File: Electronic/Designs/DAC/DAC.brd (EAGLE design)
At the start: 50 x 50 mm, 37 parts

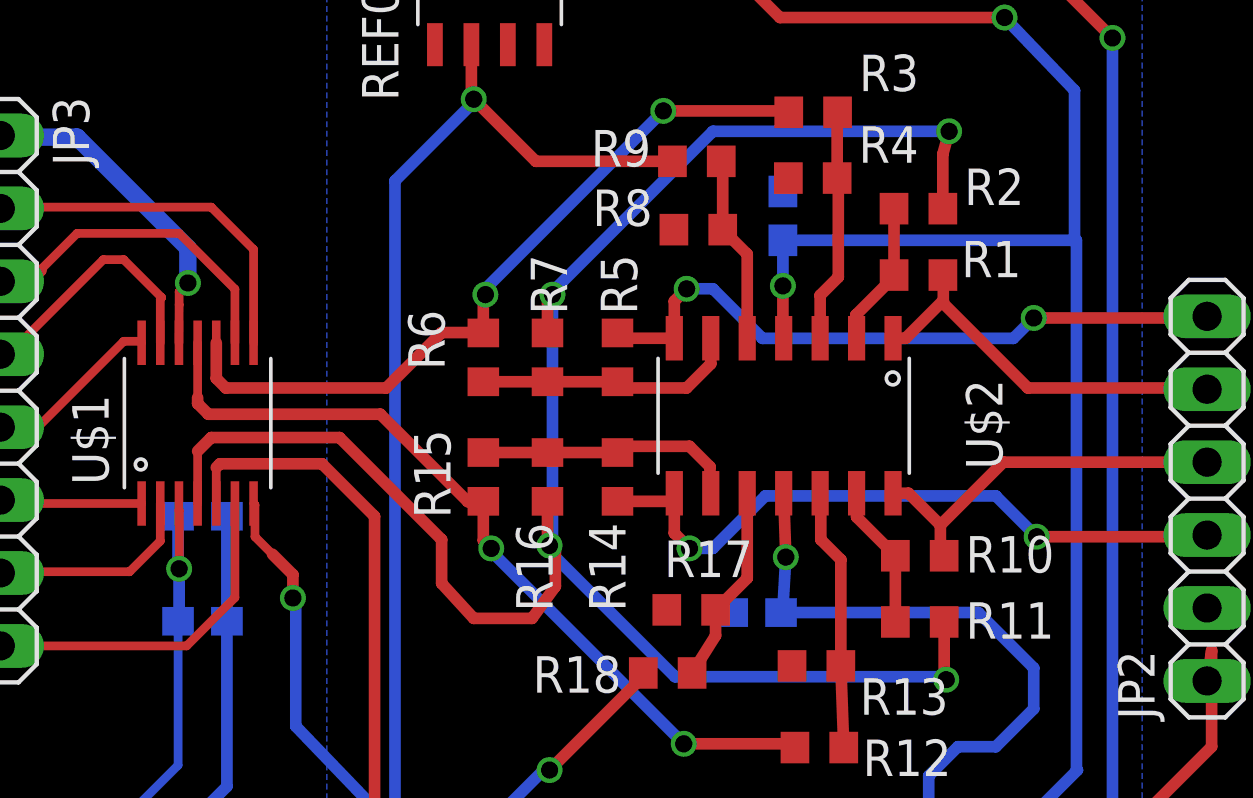
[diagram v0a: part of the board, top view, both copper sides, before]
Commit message: added dirt cheap drc / cam files , minor fix to board dac
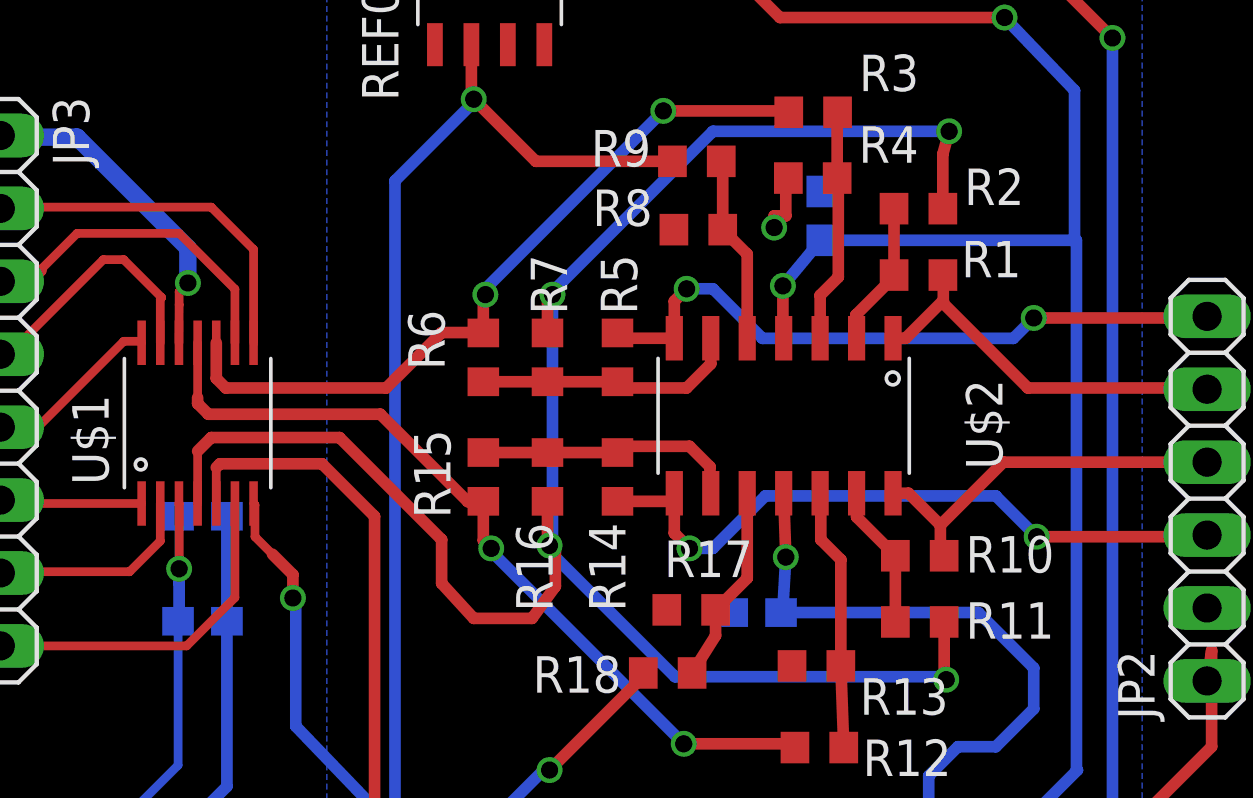
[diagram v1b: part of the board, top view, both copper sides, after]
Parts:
- moved C4 1.32 mm to (32.2, 33.3)
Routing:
- net GND: track 33.6 -> 36.3 mm, vias 1 -> 2
- net +15V: track 80.3 -> 79.5 mm
- net +5V: track 18.2 -> 19.0 mm
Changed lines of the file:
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@@
 </class>
 </classes>
-<designrules name="ITead_rule">
-<description language="de">&lt;b&gt;EAGLE Design Rules&lt;/b&gt;
-&lt;p&gt;
-Die Standard-Design-Rules sind so gewählt, dass sie für
-die meisten Anwendungen passen. Sollte ihre Platine
-besondere Anforderungen haben, treffen Sie die erforderlichen
-Einstellungen hier und speichern die Design Rules unter
-einem neuen Namen ab.</description>
-<description language="en">&lt;b&gt;EAGLE Design Rules&lt;/b&gt;
-&lt;p&gt;
-The default Design Rules have been set to cover
-a wide range of applications. Your particular design
-may have different requirements, so please make the
-necessary adjustments and save your customized
-design rules under a new name.</description>
-<description language="zh">&lt;b&gt;Seeed Studio EAGLE Design Rules&lt;/b&gt;
-</description>
+<designrules name="dirt_cheap_dirty_boards.v1">
+<description language="en">&lt;b&gt;Dirty Cheap Dirty Board Design Rules&lt;/b&gt;
+&lt;br&gt;
+&lt;br&gt;Min width/Spacing: 5/5mil
+&lt;br&gt;Min diameter of finished hole 12mil</description>
 <param name="layerSetup" value="(1*16)"/>
-<param name="mtCopper" value="0.035mm 0.035mm 0.035mm 0.035mm 0.035mm 0.035mm 0.035mm 0.035mm 0.035mm 0.035mm 0.035mm 0.035mm 0.035mm 0.035mm 0.035mm 0.035mm"/>
-<param name="mtIsolate" value="1.5mm 0.15mm 0.2mm 0.15mm 0.2mm 0.15mm 0.2mm 0.15mm 0.2mm 0.15mm 0.2mm 0.15mm 0.2mm 0.15mm 0.2mm"/>
-<param name="mdWireWire" value="6mil"/>
-<param name="mdWirePad" value="6mil"/>
-<param name="mdWireVia" value="6mil"/>
-<param name="mdPadPad" value="6mil"/>
-<param name="mdPadVia" value="6mil"/>
-<param name="mdViaVia" value="6mil"/>
+<param name="mtCopper" value="0.035mm 0.0175mm 0.035mm 0.035mm 0.035mm 0.035mm 0.035mm 0.035mm 0.035mm 0.035mm 0.035mm 0.035mm 0.035mm 0.035mm 0.0175mm 0.035mm"/>
+<param name="mtIsolate" value="1.5mm 1.1mm 0.2mm 0.15mm 0.2mm 0.15mm 0.2mm 0.15mm 0.2mm 0.15mm 0.2mm 0.15mm 0.2mm 0.15mm 0.2mm"/>
+<param name="mdWireWire" value="5mil"/>
+<param name="mdWirePad" value="5mil"/>
+<param name="mdWireVia" value="5mil"/>
+<param name="mdPadPad" value="5mil"/>
+<param name="mdPadVia" value="5mil"/>
+<param name="mdViaVia" value="5mil"/>
 <param name="mdSmdPad" value="0mil"/>
 <param name="mdSmdVia" value="0mil"/>
@@
 <param name="mdDrill" value="10mil"/>
 <param name="mdSmdStop" value="0mil"/>
-<param name="msWidth" value="6mil"/>
+<param name="msWidth" value="5mil"/>
 <param name="msDrill" value="12mil"/>
 <param name="msMicroVia" value="12mil"/>
@@
 <param name="mlMinCreamFrame" value="0mil"/>
 <param name="mlMaxCreamFrame" value="0mil"/>
-<param name="mlViaStopLimit" value="100mil"/>
+<param name="mlViaStopLimit" value="25mil"/>
 <param name="srRoundness" value="0"/>
 <param name="srMinRoundness" value="0mil"/>
@@
 <element name="C2" library="resistor" package="C0603" value="1uf" x="10.668" y="22.86" rot="MR180"/>
 <element name="C3" library="resistor" package="C0603" value="0.1uf" x="10.668" y="19.2024" rot="MR180"/>
-<element name="C4" library="resistor" package="C0603" value="1uf" x="30.8864" y="33.3248" rot="MR90"/>
+<element name="C4" library="resistor" package="C0603" value="1uf" x="32.2072" y="33.3248" rot="MR90"/>
 <element name="C5" library="resistor" package="C0603" value="1uf" x="29.972" y="19.5072" rot="MR0"/>
 <element name="C6" library="resistor" package="C0603" value="1uf" x="22.2504" y="3.1496" rot="MR0"/>
@@
 <contactref element="U$1" pad="P$3"/>
 <contactref element="C2" pad="1"/>
-<wire x1="9.8484" y1="23.07" x2="9.8552" y2="23.0632" width="0.3048" layer="1"/>
-<wire x1="9.8552" y1="23.0632" x2="9.8552" y2="21.0312" width="0.3048" layer="1"/>
 <via x="9.8552" y="21.0312" extent="1-16" drill="0.6"/>
 <contactref element="JP4" pad="2"/>
@@
 <wire x1="7.112" y1="11.4808" x2="3.5052" y2="11.4808" width="0.3048" layer="16"/>
 <wire x1="3.5052" y1="11.4808" x2="3.4544" y2="11.43" width="0.3048" layer="16"/>
-<wire x1="9.8552" y1="19.2396" x2="9.8552" y2="21.0312" width="0.4064" layer="16"/>
-<wire x1="9.818" y1="22.86" x2="9.818" y2="21.0684" width="0.4064" layer="16"/>
+<wire x1="9.8552" y1="19.2396" x2="9.8552" y2="20.5232" width="0.4064" layer="16"/>
+<wire x1="9.8552" y1="20.5232" x2="9.8552" y2="21.0312" width="0.4064" layer="16"/>
 <wire x1="9.818" y1="21.0684" x2="9.8552" y2="21.0312" width="0.4064" layer="16"/>
-<wire x1="9.8484" y1="23.07" x2="9.8484" y2="23.3056" width="0" layer="19" extent="1-1"/>
+<wire x1="9.8484" y1="23.3056" x2="9.8552" y2="23.3056" width="0.3048" layer="1"/>
+<wire x1="9.8552" y1="23.3056" x2="9.8552" y2="21.0312" width="0.3048" layer="1"/>
+<wire x1="9.818" y1="22.86" x2="9.8552" y2="22.86" width="0.3048" layer="16"/>
+<wire x1="9.8552" y1="22.86" x2="9.8552" y2="20.5232" width="0.3048" layer="16"/>
 <wire x1="9.818" y1="19.2024" x2="9.8552" y2="19.2396" width="0" layer="19" extent="16-16"/>
 </signal>
@@
 <wire x1="30.8864" y1="29.0624" x2="30.8864" y2="30.8864" width="0.4064" layer="1"/>
 <via x="30.8864" y="30.8864" extent="1-16" drill="0.6"/>
-<wire x1="30.8864" y1="30.8864" x2="30.8864" y2="32.4748" width="0.4064" layer="16"/>
+<wire x1="30.8864" y1="30.8864" x2="32.2072" y2="32.4748" width="0.4064" layer="16"/>
 <wire x1="30.7848" y1="10.2616" x2="32.8168" y2="10.2616" width="0.4064" layer="1"/>
 <wire x1="32.8168" y1="10.2616" x2="34.9504" y2="12.3952" width="0.4064" layer="1"/>
@@
 <wire x1="30.7848" y1="40.2336" x2="27.6352" y2="43.3832" width="0.4064" layer="1"/>
 <wire x1="27.6352" y1="43.3832" x2="27.6352" y2="45.8216" width="0.4064" layer="1"/>
-<wire x1="30.8864" y1="32.4748" x2="41.0464" y2="32.4748" width="0.4064" layer="16"/>
+<wire x1="32.2072" y1="32.4748" x2="41.0464" y2="32.4748" width="0.4064" layer="16"/>
 <wire x1="41.148" y1="14.0208" x2="41.1108" y2="14.0208" width="0.4064" layer="16"/>
 <wire x1="41.1108" y1="14.0208" x2="41.1108" y2="32.4748" width="0.4064" layer="16"/>
@@
 <wire x1="9.8552" y1="30.2264" x2="9.8552" y2="30.6832" width="0.3048" layer="1"/>
 <wire x1="9.8552" y1="30.6832" x2="10.16" y2="30.988" width="0.3048" layer="1"/>
-<wire x1="31.0768" y1="34.642" x2="30.8864" y2="34.1748" width="0" layer="19" extent="1-16"/>
+<wire x1="31.0768" y1="34.642" x2="30.988" y2="34.642" width="0.4064" layer="1"/>
+<wire x1="30.988" y1="34.642" x2="30.988" y2="33.3248" width="0.4064" layer="1"/>
+<wire x1="30.988" y1="33.3248" x2="30.5816" y2="33.3248" width="0.4064" layer="1"/>
+<wire x1="30.5816" y1="33.3248" x2="30.5816" y2="32.9184" width="0.4064" layer="1"/>
+<via x="30.5816" y="32.9184" extent="1-16" drill="0.6"/>
+<wire x1="30.5816" y1="32.9184" x2="30.5816" y2="33.02" width="0.4064" layer="16"/>
+<wire x1="30.5816" y1="33.02" x2="30.6832" y2="33.02" width="0.4064" layer="16"/>
+<wire x1="30.6832" y1="33.02" x2="30.6832" y2="33.3248" width="0.4064" layer="16"/>
 </signal>
 <signal name="XPOS">
